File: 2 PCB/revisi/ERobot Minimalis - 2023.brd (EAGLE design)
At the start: 16 parts, among them J1 215297-6, J2 215297-6, J3 1935161, J4 215297-6, U1 STMICROELECTRONICS_L7805CVSTM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, U2 STMICROELECTRONICS_L7805CVSTM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

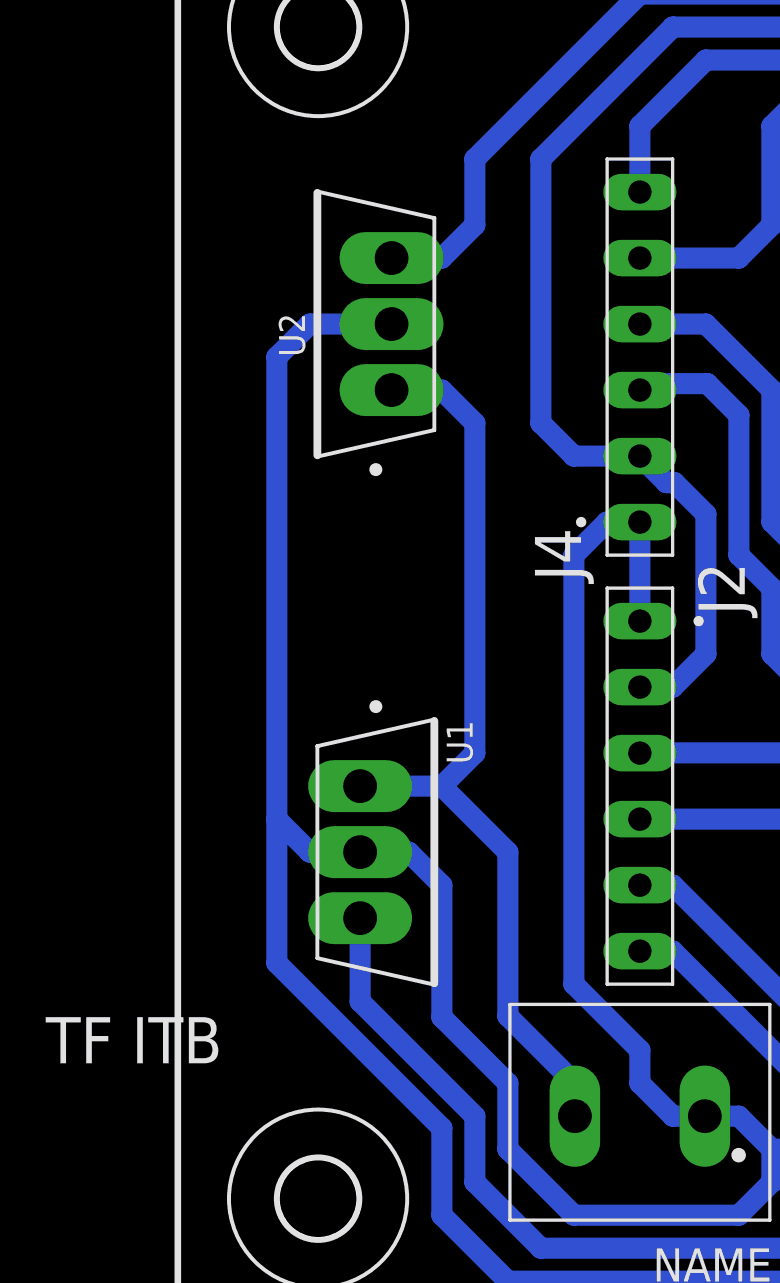
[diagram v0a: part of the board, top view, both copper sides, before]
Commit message: tambah 1 baterai PCB
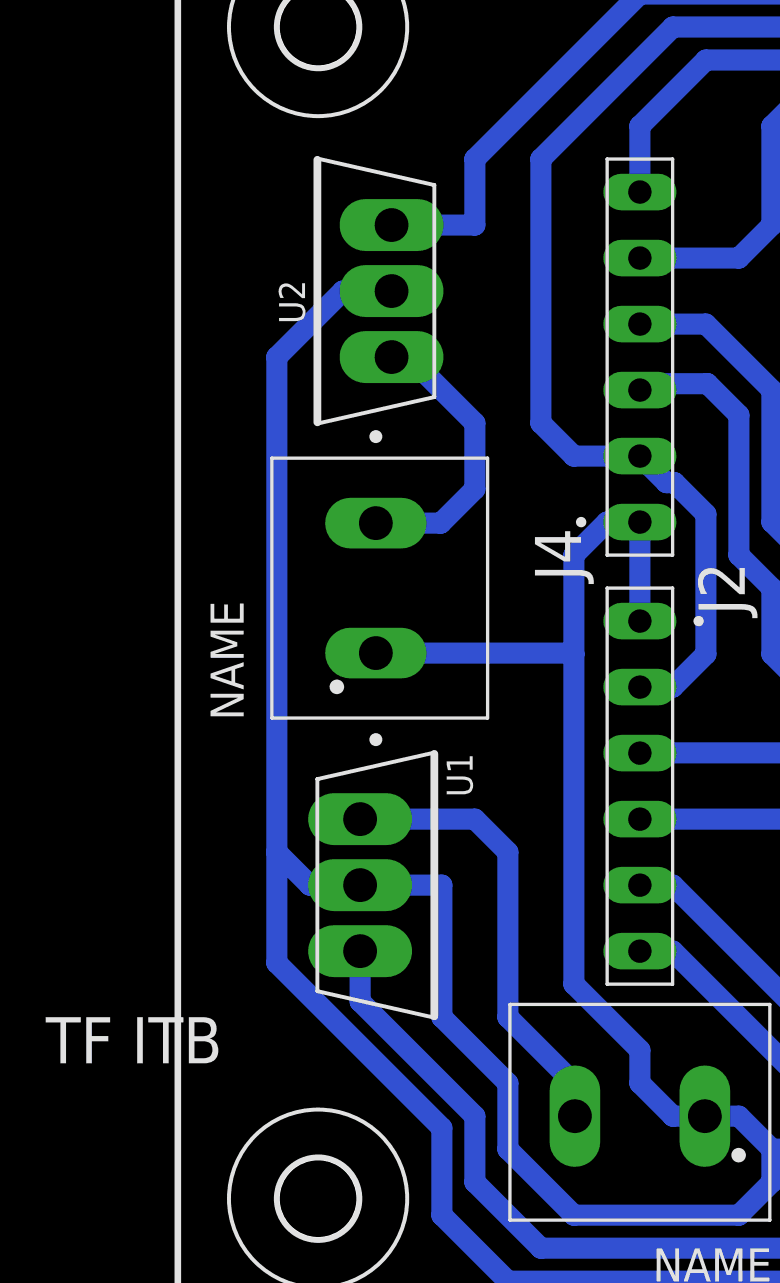
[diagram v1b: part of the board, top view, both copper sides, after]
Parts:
- added J5: 1935161, 1935161:PHOENIX_1935161
- moved U2 1.27 mm to (7.62, 40.6)
- moved U1 1.27 mm to (7.62, 17.8)
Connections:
- new net N$2: J3.2, U1.1
- net GND: now also J5.1
- net N$1: now also J5.2; no longer J3.2, U1.1
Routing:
- net N$1: track 36.2 -> 11.1 mm
- net N$2: track 0.00 -> 17.4 mm
- net GND: track 256.5 -> 264.1 mm
- net +5V: track 241.2 -> 239.4 mm
